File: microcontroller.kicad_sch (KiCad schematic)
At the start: 20 parts, among them U1 RP2350A, X1 ABM8-272-T3

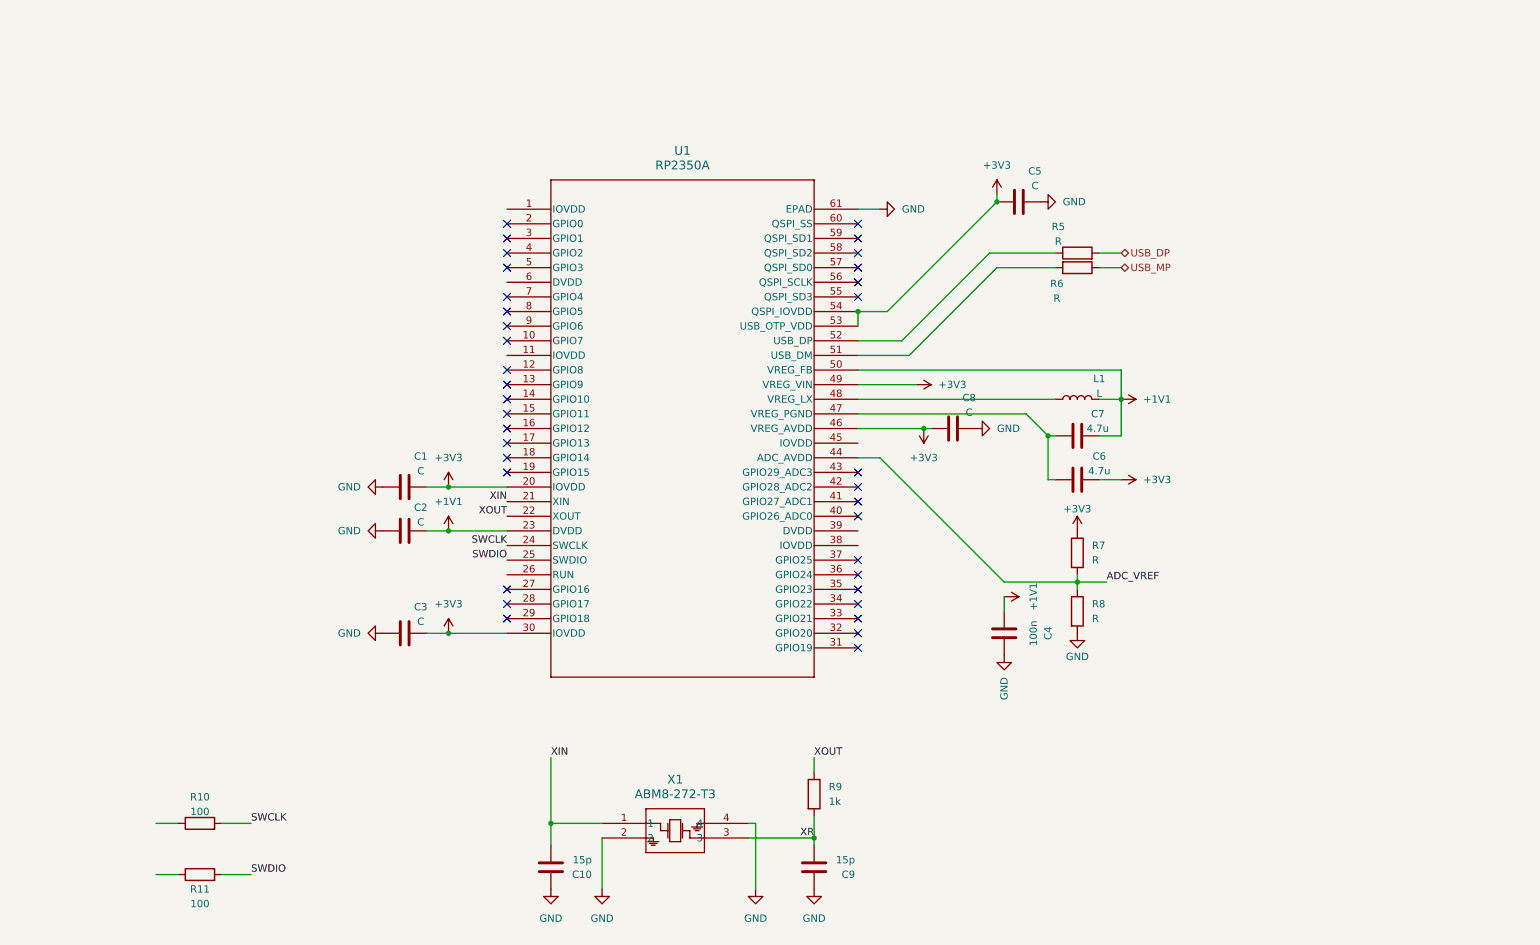
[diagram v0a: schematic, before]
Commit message: Updating schematic and adding in compnents to the PCB
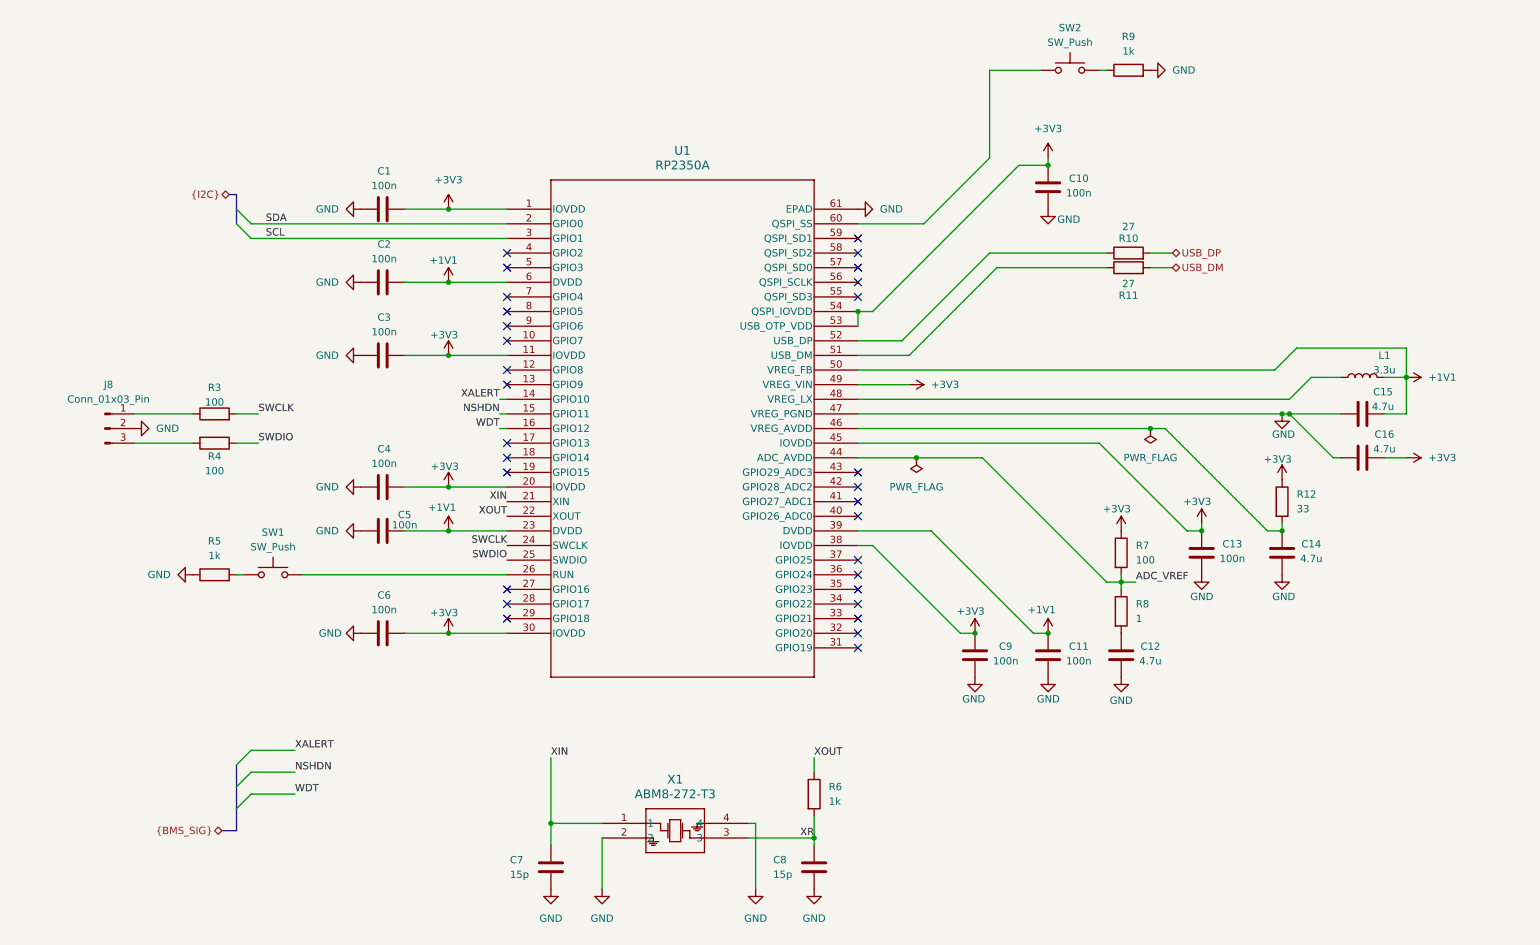
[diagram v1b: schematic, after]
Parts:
- removed C8: C, symbol Device:C
- removed R6: R, symbol Device:R
- added C10, C11, C13, C6, C9: 100n, Capacitor_SMD:C_0201_0603Metric, symbol Device:C
- added C12, C14: 4.7u, Capacitor_SMD:C_0402_1005Metric, symbol Device:C
- added J8: Conn_01x03_Pin, Connector_JST:JST_SH_SM03B-SRSS-TB_1x03-1MP_P1.00mm_Horizontal, symbol Connector:Conn_01x03_Pin
- added R12: 33, Resistor_SMD:R_0402_1005Metric, symbol Device:R
- added R4: 100, Resistor_SMD:R_0201_0603Metric, symbol Device:R
- added R5, R9: 1k, Resistor_SMD:R_0402_1005Metric, symbol Device:R
- added SW1, SW2: SW_Push, _BMS:SW_TS02-66-43-BK-160-LCR-D, symbol Switch:SW_Push
- C1, C2, C3, C5: value C -> 100n; footprint (none) -> Capacitor_SMD:C_0201_0603Metric; Mfr (none) -> Murata Electronics; Mfr P/N (none) -> GRT033R60J104KE01D; Supplier_1 (none) -> Digikey; Supplier_1 P/N (none) -> 490-16306-2-ND; Supplier_1 Price @ Qty (none) -> 1; Supplier_1 Unit Price (none) -> 0.10000
- C4: footprint (none) -> Capacitor_SMD:C_0201_0603Metric; Mfr (none) -> Murata Electronics; Mfr P/N (none) -> GRT033R60J104KE01D; Supplier_1 (none) -> Digikey; Supplier_1 P/N (none) -> 490-16306-2-ND; Supplier_1 Price @ Qty (none) -> 1; Supplier_1 Unit Price (none) -> 0.10000
- L1: value L -> 3.3u; footprint (none) -> Inductor_SMD:L_0805_2012Metric; Mfr (none) -> Abracon LLC; Mfr P/N (none) -> AOTA-B201610S3R3-101-T; Supplier_1 (none) -> Digikey; Supplier_1 P/N (none) -> 535-AOTA-B201610S3R3-101-TTR-ND; Supplier_1 Price @ Qty (none) -> 1; Supplier_1 Unit Price (none) -> 0.22000
- R10: renamed from R5; value R -> 27; footprint (none) -> Resistor_SMD:R_0201_0603Metric; Mfr (none) -> YAGEO; Mfr P/N (none) -> RC0201FR-0727RL; Supplier_1 (none) -> Digikey; Supplier_1 P/N (none) -> YAG2554TR-ND; Supplier_1 Price @ Qty (none) -> 1; Supplier_1 Unit Price (none) -> 0.10000
- R11: value 100 -> 27; footprint (none) -> Resistor_SMD:R_0201_0603Metric; Mfr (none) -> YAGEO; Mfr P/N (none) -> RC0201FR-0727RL; Supplier_1 (none) -> Digikey; Supplier_1 P/N (none) -> YAG2554TR-ND; Supplier_1 Price @ Qty (none) -> 1; Supplier_1 Unit Price (none) -> 0.10000
- R3: renamed from R10; footprint (none) -> Resistor_SMD:R_0201_0603Metric; Mfr (none) -> YAGEO; Mfr P/N (none) -> AC0201FR-07100RL; Supplier_1 (none) -> Digikey; Supplier_1 P/N (none) -> YAG3412TR-ND; Supplier_1 Price @ Qty (none) -> 1; Supplier_1 Unit Price (none) -> 0.10000
- R7: value R -> 100; footprint (none) -> Capacitor_SMD:C_0402_1005Metric; Mfr (none) -> YAGEO; Mfr P/N (none) -> RC0402FR-07100RL; Supplier_1 (none) -> Digikey; Supplier_1 P/N (none) -> 311-100LRTR-ND; Supplier_1 Price @ Qty (none) -> 1; Supplier_1 Unit Price (none) -> 0.10000
- R8: value R -> 1; footprint (none) -> Resistor_SMD:R_0402_1005Metric; Mfr (none) -> Stackpole Electronics Inc; Mfr P/N (none) -> RMCF0402FT1R00; Supplier_1 (none) -> Digikey; Supplier_1 P/N (none) -> 738-RMCF0402FT1R00TR-ND; Supplier_1 Price @ Qty (none) -> 1; Supplier_1 Unit Price (none) -> 0.10000
- U1: footprint QFN-60_7X7_RPI -> _BMS:QFN-60_7X7_RPI
- X1: footprint ABM8-272-T3_ABR -> _BMS:ABM8-272-T3_ABR
- renumbered C7 to C15, C6 to C16, C10 to C7, C9 to C8, R9 to R6
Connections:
- net +1V1: now also C5.2, U1.39 (DVDD), U1.6 (DVDD), C11.1; no longer C4.1
- net +3V3: now also C4.2, U1.1 (IOVDD), U1.11 (IOVDD), U1.38 (IOVDD), U1.45 (IOVDD), C10.1, C13.1, C6.2, C9.1, R12.1; no longer C5.1, U1.46 (VREG_AVDD)
- net GND: now also C15.1, C16.1, C4.1, C5.1, C7.2, C8.2, U1.47 (VREG_PGND), C10.2, C11.2, C12.2, C13.2, C14.2, C6.1, C9.2, J8.2 (Pin_2), R5.1, R9.2; no longer C4.2, C5.2, C7.1, C8.1, R8.2
- net SWDIO: now also R4.1; no longer R11.2
- net XIN: now also C7.1; no longer C7.2
- net XR: now also C8.1; no longer C8.2
- net at R3.1: now also J8.1 (Pin_1)
- net XALERT: now reaches U1.14 (GPIO10)
- net NSHDN: now reaches U1.15 (GPIO11)
- net WDT: now reaches U1.16 (GPIO12)
- net SDA: now reaches U1.2 (GPIO0)
- net at U1.26 (RUN): now also SW1.2
- net SCL: now reaches U1.3 (GPIO1)
- net at U1.51 (USB_DM): now also R11.1
- net at U1.60 (QSPI_SS): now also SW2.1
- new net: C12.1, R8.2
- new net: R5.2, SW1.1
- new net: R9.1, SW2.2
- new net: J8.3 (Pin_3), R4.2
- new net: C14.1, R12.2, U1.46 (VREG_AVDD)
- new net USB_DM: R11.2
- no-connect marks 36 -> 30
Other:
- moved on the sheet: C15, C16, C7, C8, L1, R10, R3, R7, R8

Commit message: schematic progress
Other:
- moved on the sheet: R12
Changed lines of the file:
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@@
 	(wire
 		(pts
+			(xy 231.14 99.06) (xy 231.14 100.33)
+		)
+		(stroke
+			(width 0)
+			(type default)
+		)
+	)
+	(wire
+		(pts
 			(xy 49.53 87.63) (xy 53.34 87.63)
 		)
@@
 	(symbol
 		(lib_id "Device:R")
-		(at 231.14 102.87 0)
+		(at 231.14 104.14 0)
 		(unit 1)
 		(exclude_from_sim no)
@@
 		(fields_autoplaced yes)
 		(property "Reference" "R12"
-			(at 233.68 101.5999 0)
+			(at 233.68 102.8699 0)
 			(effects
 				(font
@@
 		)
 		(property "Value" "33"
-			(at 233.68 104.1399 0)
+			(at 233.68 105.4099 0)
 			(effects
 				(font
@@
 		)
 		(property "Footprint" "Resistor_SMD:R_0402_1005Metric"
-			(at 229.362 102.87 90)
+			(at 229.362 104.14 90)
 			(effects
 				(font
@@
 		)
 		(property "Datasheet" "https://www.yageogroup.com/content/Resource%20Library/Datasheet/PYU-PE_521_ROHS_L.pdf"
-			(at 231.14 102.87 0)
+			(at 231.14 104.14 0)
 			(effects
 				(font
@@
 		)
 		(property "Description" "RES 0.033 OHM 1% 1/16W 0402"
-			(at 231.14 102.87 0)
+			(at 231.14 104.14 0)
 			(effects
 				(font
@@
 		)
 		(property "Mfr" "PE0402FRF070R033L"
-			(at 231.14 102.87 0)
+			(at 231.14 104.14 0)
 			(effects
 				(font
@@
 		)
 		(property "Mfr P/N" "YAGEO"
-			(at 231.14 102.87 0)
+			(at 231.14 104.14 0)
 			(effects
 				(font
@@
 		)
 		(property "Supplier_1" "Digikey"
-			(at 231.14 102.87 0)
+			(at 231.14 104.14 0)
 			(effects
 				(font
@@
 		)
 		(property "Supplier_1 P/N" "13-PE0402FRF070R033LTR-ND"
-			(at 231.14 102.87 0)
+			(at 231.14 104.14 0)
 			(effects
 				(font
@@
 		)
 		(property "Supplier_1 Unit Price" "0.54000"
-			(at 231.14 102.87 0)
+			(at 231.14 104.14 0)
 			(effects
 				(font
@@
 		)
 		(property "Supplier_1 Price @ Qty" "1"
-			(at 231.14 102.87 0)
+			(at 231.14 104.14 0)
 			(effects
 				(font
@@
 		)
 		(property "Supplier_2" ""
-			(at 231.14 102.87 0)
+			(at 231.14 104.14 0)
 			(effects
 				(font
@@
 		)
 		(property "Supplier_2 P/N" ""
-			(at 231.14 102.87 0)
+			(at 231.14 104.14 0)
 			(effects
 				(font
@@
 		)
 		(property "Supplier_2 Unit Price" ""
-			(at 231.14 102.87 0)
+			(at 231.14 104.14 0)
 			(effects
 				(font
@@
 		)
 		(property "Supplier_2 Price @ Qty" ""
-			(at 231.14 102.87 0)
+			(at 231.14 104.14 0)
 			(effects
 				(font

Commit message: Layed on board. Still need to route
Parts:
- removed C4: 100n, Capacitor_SMD:C_0201_0603Metric, symbol Device:C
- renumbered C11 to C10, C12 to C11, C13 to C12, C14 to C13, C15 to C14, C16 to C15, C5 to C4, C6 to C5, C7 to C6, C8 to C7, C9 to C8, C10 to C9, J8 to J4, U1 to U3
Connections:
- net +3V3: no longer U3.20 (IOVDD)
- no-connect marks 30 -> 31
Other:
- moved on the sheet: R12

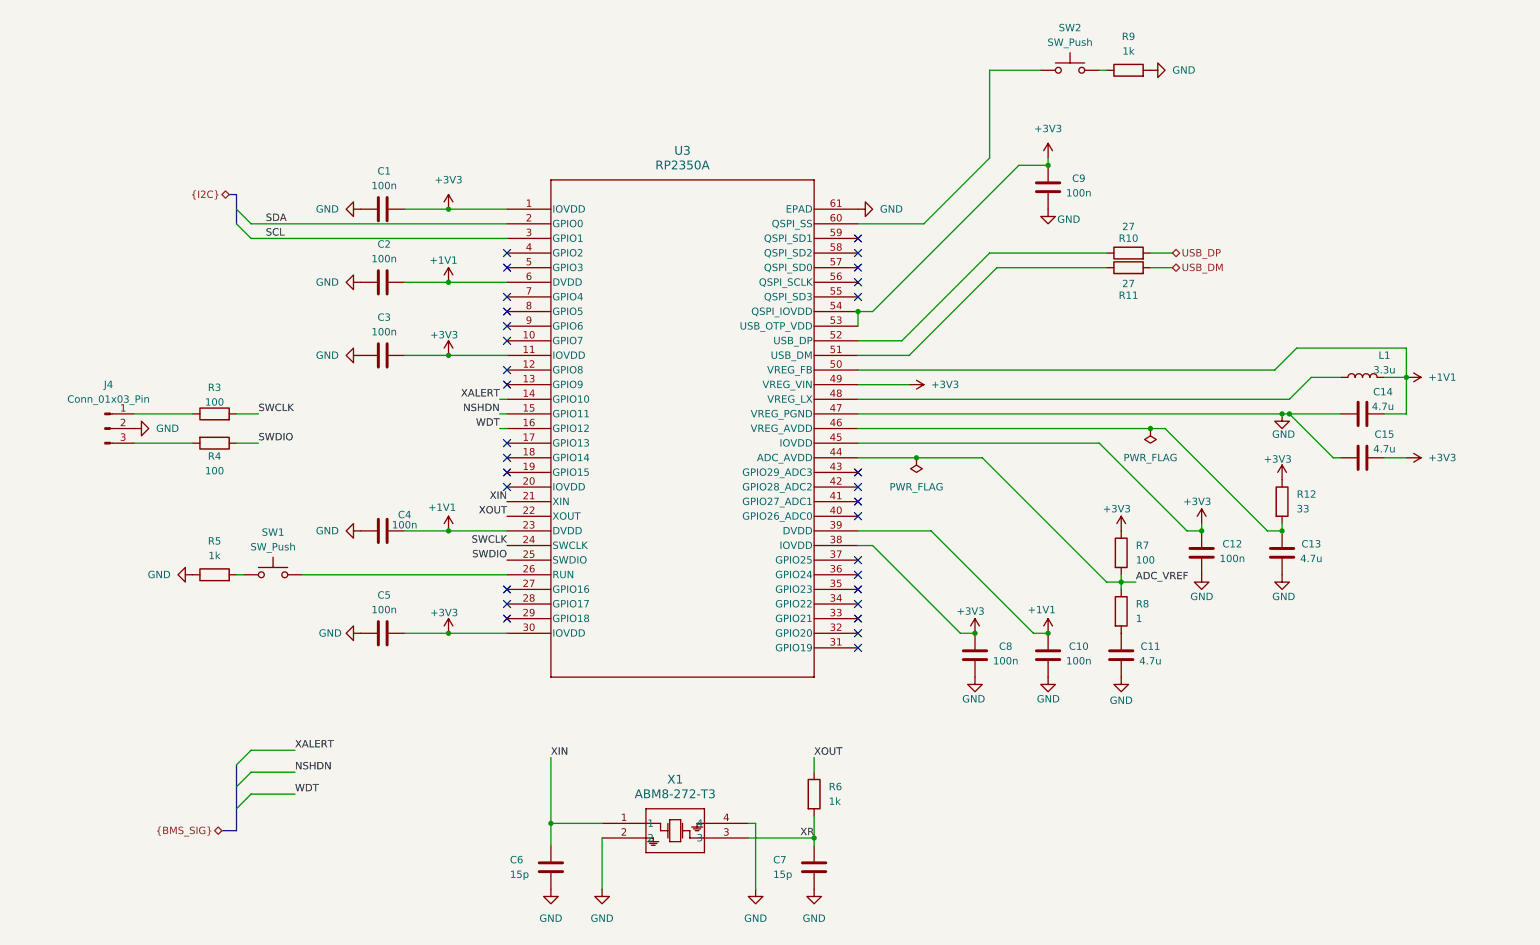
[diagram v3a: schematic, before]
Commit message: Adding proper grounding
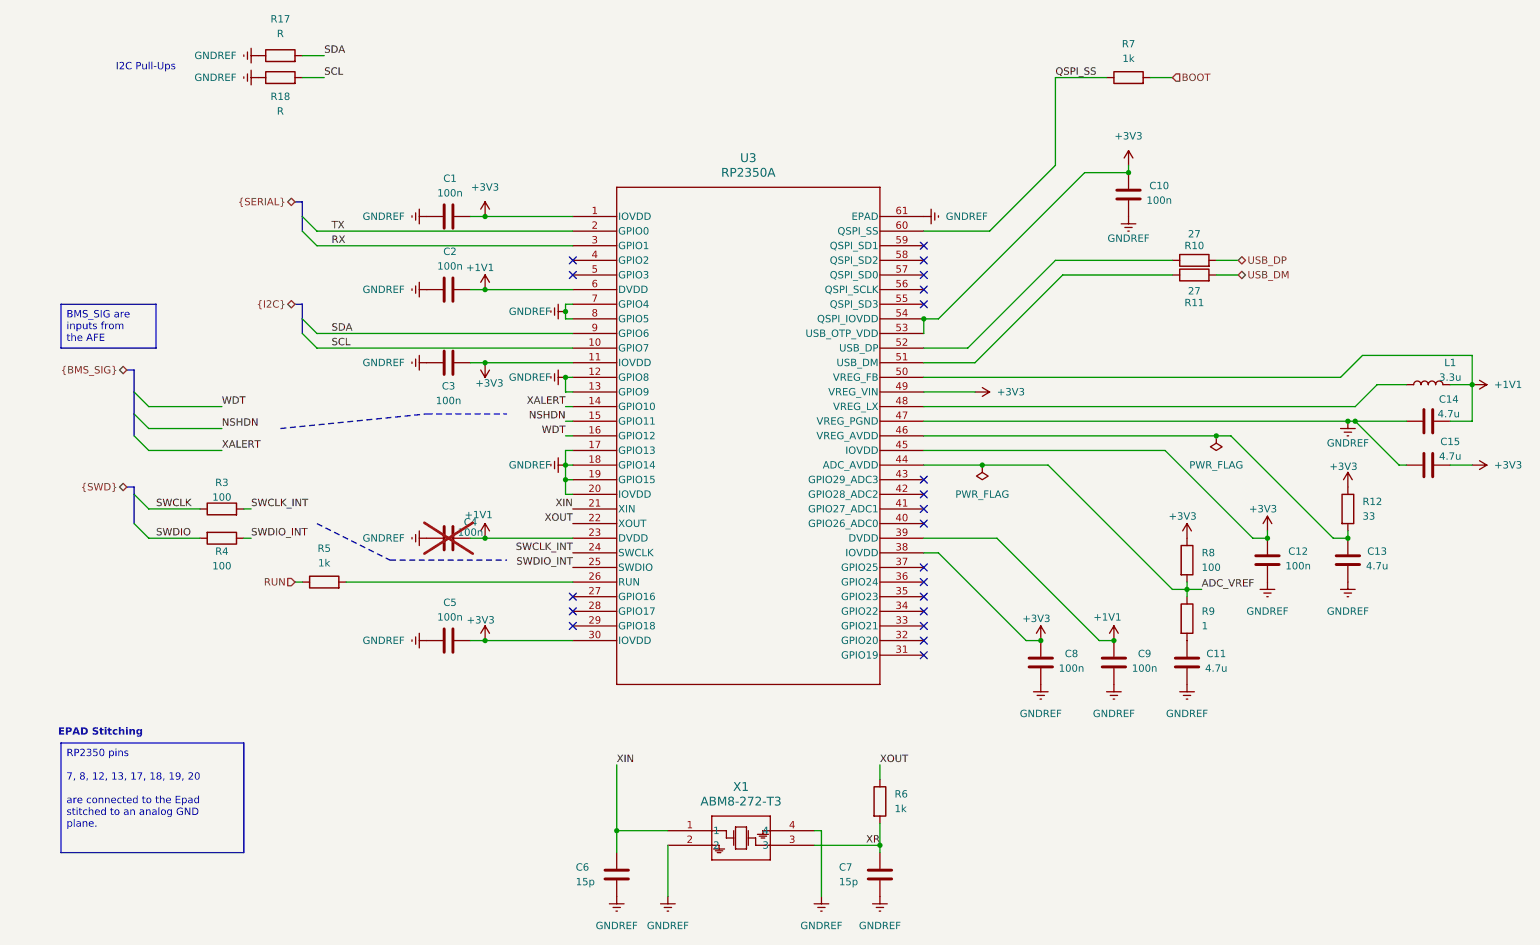
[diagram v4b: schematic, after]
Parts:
- removed J4: Conn_01x03_Pin, Connector_JST:JST_SH_SM03B-SRSS-TB_1x03-1MP_P1.00mm_Horizontal, symbol Connector:Conn_01x03_Pin
- removed SW1, SW2: SW_Push, _BMS:SW_TS02-66-43-BK-160-LCR-D, symbol Switch:SW_Push
- added R17, R18: R, symbol Device:R
- C4: now not fitted; now left out of the parts list
- renumbered C9 to C10, C10 to C9, R9 to R7, R7 to R8, R8 to R9
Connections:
- net SCL: now also U3.10 (GPIO7), R18.2; no longer U3.3 (GPIO1)
- net SDA: now also U3.9 (GPIO6), R17.2; no longer U3.2 (GPIO0)
- net SWCLK: now also R3.1; no longer R3.2, U3.24 (SWCLK)
- net SWDIO: now also R4.2; no longer R4.1, U3.25 (SWDIO)
- net at R5.2: now also U3.26 (RUN)
- net QSPI_SS: now reaches R7.1
- net QSPI_SS: now also U3.60 (QSPI_SS)
- net GNDREF: now reaches U3.12 (GPIO8)
- net GNDREF: now also C1.1, C10.2, C11.2, C12.2, C13.2, C14.1, C15.1, C2.1, C3.1, C4.1, C5.1, C6.2, C7.2, C8.2, C9.2, U3.13 (GPIO9), U3.17 (GPIO13), U3.18 (GPIO14), U3.19 (GPIO15), U3.20 (IOVDD), U3.47 (VREG_PGND), U3.61 (EPAD), U3.7 (GPIO4), U3.8 (GPIO5), X1.2, X1.4, R17.1, R18.1
- removed net GND: C1.1, C10.2, C11.2, C12.2, C13.2, C14.1, C15.1, C2.1, C3.1, C4.1, C5.1, C6.2, C7.2, C8.2, C9.2, R5.1, R7.2, U3.47 (VREG_PGND), U3.61 (EPAD), X1.2, X1.4
- new net BOOT: R7.2
- new net RUN: R5.1
- new net RX: U3.3 (GPIO1)
- new net SWCLK_INT: R3.2, U3.24 (SWCLK)
- new net SWDIO_INT: R4.1, U3.25 (SWDIO)
- new net TX: U3.2 (GPIO0)
- no-connect marks 31 -> 21
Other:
- note added: "EPAD Stitching"
- note added: "I2C Pull-Ups"
- moved on the sheet: C1, C10, C11, C12, C13, C14, C15, C2, C3, C5, C6, C7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

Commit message: Lots of changfes
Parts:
- removed R18: R, symbol Device:R
- removed R8: 100, Capacitor_SMD:C_0402_1005Metric, symbol Device:R
- removed R9: 1, Resistor_SMD:R_0402_1005Metric, symbol Device:R
- added C4: 100n, Capacitor_SMD:C_0201_0603Metric, symbol Device:C
- added R6: R, Resistor_SMD:R_0402_1005Metric, symbol Device:R
- C5: renamed from C4; now fitted; now in the parts list
- R5: renamed from R17; footprint (none) -> Resistor_SMD:R_0402_1005Metric; Mfr (none) -> KOA Speer Electronics, Inc.; Mfr P/N (none) -> RN73R1ETTP3302B25; Supplier_1 (none) -> Digikey; Supplier_1 P/N (none) -> 2019-RN73R1ETTP3302B25TR-ND; Supplier_1 Price @ Qty (none) -> 1; Supplier_1 Unit Price (none) -> 0.10000
- renumbered C9 to C10, C10 to C11, C11 to C12, C12 to C13, C13 to C14, C14 to C15, C15 to C16, C5 to C6, C6 to C7, C7 to C8, C8 to C9, R5 to R7, R6 to R8, R7 to R9
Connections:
- net ADC_VREF is gone; now on net +3V3: U3.44 (ADC_AVDD)
- net +3V3: now also C12.1, U3.20 (IOVDD), C4.2
- net SCL: now also R6.1
- net D+: now reaches R10.1, U3.52 (USB_DP)
- net D-: now reaches R11.1, U3.51 (USB_DM)
- net GNDREF renamed GND
- net GND: now also C4.1, R6.2; no longer U3.20 (IOVDD)
- net USB_DM renamed USB_D-
- net USB_DP renamed USB_D+
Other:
- moved on the sheet: C12

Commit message: Tweaks and production files
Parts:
- added J9: Conn_01x02_Socket, Connector_JST:JST_PH_B2B-PH-K_1x02_P2.00mm_Vertical, symbol Connector:Conn_01x02_Socket
- R5, R6: value R -> 33k

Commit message: Updating BOM
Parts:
- C1, C10, C11, C13, C2, C3, C4, C5, C6, C9: value 100n -> 100 nF; footprint Capacitor_SMD:C_0201_0603Metric -> Capacitor_SMD:C_0402_1005Metric; Mfr P/N GRT033R60J104KE01D -> GRM155C71H104JE19D; Supplier_1 Digikey -> DigiKey; Supplier_1 P/N 490-16306-2-ND -> 490-GRM155C71H104JE19DTR-ND; Supplier_1 Price @ QTY (none) -> 1; Supplier_1 Price @ Qty 1 -> (none)
- R12: Mfr PE0402FRF070R033L -> Vishay Dale; Mfr P/N YAGEO -> TNPW040233R0DEED; Supplier_1 P/N 13-PE0402FRF070R033LTR-ND -> 541-TNPW040233R0DEEDTR-ND; Supplier_1 Unit Price 0.54000 -> 0.20000
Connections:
- net +1V1: now also C10.2, C2.1, C5.1; no longer C10.1, C2.2, C5.2
- net +3V3: now also C1.1, C11.2, C13.2, C3.1, C4.1, C6.1, C9.2; no longer C1.2, C11.1, C13.1, C3.2, C4.2, C6.2, C9.1
- net GND: now also C1.2, C10.1, C11.1, C13.1, C2.2, C3.2, C4.2, C5.2, C6.2, C9.1; no longer C1.1, C10.2, C11.2, C13.2, C2.1, C3.1, C4.1, C5.1, C6.1, C9.2
